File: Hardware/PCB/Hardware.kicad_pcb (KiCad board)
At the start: 2 copper layers, 68.6 x 53.3 mm, 33 parts, among them J1 Conn_01x03_Male, M1 Motor_Servo, M2 Motor_Servo, M3 Motor_Servo, P1 Power, P2 Analog, P3 Digital, P4 Digital, P5 CONN_01X01, P6 CONN_01X01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

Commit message: Nouveau PCB simplifié
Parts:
- removed RV1: R_POT, Potentiometer_THT:Potentiometer_Alps_RK09L_Single_Vertical
- removed SW1: SW_Push, Button_Switch_THT:SW_PUSH_6mm
- added R11: R, Resistor_THT:R_Axial_DIN0204_L3.6mm_D1.6mm_P2.54mm_Vertical, F.Cu at (174.5, 84.5)
- BZ1: footprint Buzzer_Beeper:MagneticBuzzer_Kingstate_KCG0601 -> Connector_PinHeader_2.54mm:PinHeader_1x02_P2.54mm_Horizontal
- R1: footprint Resistor_THT:R_Axial_DIN0204_L3.6mm_D1.6mm_P1.90mm_Vertical -> Resistor_THT:R_Axial_DIN0204_L3.6mm_D1.6mm_P2.54mm_Vertical
- R2, R4, R6, R8: footprint Connector_JST:JST_XH_B02B-XH-A_1x02_P2.50mm_Vertical -> Connector_PinHeader_2.54mm:PinHeader_1x02_P2.54mm_Vertical
- moved D4 63.6 mm to (174.5, 81.4)
- moved R10 48.6 mm to (156.7, 84.5), turned to 270 degrees
- moved D5 42.8 mm to (156.7, 81.9)
- moved R1 36.0 mm to (154.2, 89.5), turned to 180 degrees
- moved U3 26.4 mm to (132.6, 111.1)
- moved D1 25.3 mm to (145.3, 108.6), turned to 90 degrees
- moved R2 21.7 mm to (164.3, 107.3), turned to 0 degrees
- moved R6 18.0 mm to (168.1, 107.3), turned to 0 degrees
- moved M3 17.6 mm to (175.8, 97.2), turned to 270 degrees
- moved U1 15.2 mm to (132.6, 98.4), turned to 0 degrees
- moved BZ1 14.9 mm to (155.4, 98.4), turned to 0 degrees
- moved R8 14.2 mm to (172.0, 107.3), turned to 0 degrees
- moved R4 12.7 mm to (160.5, 107.3), turned to 0 degrees
- moved R9 12.0 mm to (169.4, 120.0), turned to 0 degrees
- moved D3 10.5 mm to (145.3, 95.9), turned to 90 degrees
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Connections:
- D4 pad 2: /7 -> /2
- D5 pad 1: Net-(D4-Pad1) -> Net-(D5-Pad1)
- J1 pad 1: Net-(J1-Pad1) -> +5V
- M1 pad 2: Net-(M1-Pad2) -> +5V
- M2 pad 2: Net-(M1-Pad2) -> +5V
- M3 pad 2: Net-(M1-Pad2) -> +5V
- P3 pad 5: /13(SCK) -> Net-(P3-Pad5)
- R1 pad 1: /A4(SDA) -> Net-(BZ1-Pad1)
- R1 pad 2: Net-(J1-Pad2) -> /9(**)
- R10 pad 1: Net-(D4-Pad1) -> Net-(D5-Pad1)
- R2 pad 1: /13(SCK) -> +5V
- R4 pad 1: /13(SCK) -> +5V
- R6 pad 1: /13(SCK) -> +5V
- R8 pad 1: /13(SCK) -> +5V
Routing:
- net +5V: track 67.8 -> 157.7 mm, vias 2 -> 0
- net /13(SCK): track 69.4 -> 0.00 mm
- net /12(MISO): track 64.0 -> 0.00 mm
- net /7: track 67.1 -> 3.81 mm, vias 2 -> 0
- net /A4(SDA): track 38.2 -> 0.15 mm
- net Net-(M1-Pad2): track 32.3 -> 0.00 mm
- net /8: track 15.1 -> 45.9 mm
- net /3(**): track 51.0 -> 25.3 mm
- net /9(**): track 37.9 -> 18.2 mm
- net /A1: track 28.6 -> 14.0 mm
- net Net-(BZ1-Pad1): track 23.0 -> 9.42 mm
- net Net-(J1-Pad2): track 10.8 -> 0.00 mm
- net Net-(D4-Pad1): track 13.4 -> 3.03 mm
- net /A2: track 24.2 -> 14.5 mm
- net /10(**/SS): track 26.0 -> 35.6 mm
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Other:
- net class Default: trace_width 0.25 -> 0.4

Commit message: PCB corrigé et verifié. Typon prêt
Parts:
- added R12: R, Resistor_THT:R_Axial_DIN0204_L3.6mm_D1.6mm_P5.08mm_Horizontal, F.Cu at (145.3, 93.3)
- added R13: R, Resistor_THT:R_Axial_DIN0204_L3.6mm_D1.6mm_P5.08mm_Horizontal, F.Cu at (145.3, 106.0)
- added R14: R, Resistor_THT:R_Axial_DIN0204_L3.6mm_D1.6mm_P5.08mm_Horizontal, F.Cu at (128.8, 90.8)
- D1, D3: footprint Diode_THT:D_DO-15_P5.08mm_Vertical_KathodeUp -> Diode_THT:D_T-1_P10.16mm_Horizontal
- D2: footprint Diode_THT:D_A-405_P5.08mm_Vertical_KathodeUp -> Diode_THT:D_T-1_P10.16mm_Horizontal
- J1: footprint Connector_PinHeader_1.27mm:PinHeader_1x03_P1.27mm_Horizontal -> Connector_PinHeader_2.54mm:PinHeader_1x03_P2.54mm_Horizontal
- R3, R7: footprint Resistor_THT:R_Axial_DIN0204_L3.6mm_D1.6mm_P1.90mm_Vertical -> Resistor_THT:R_Axial_DIN0204_L3.6mm_D1.6mm_P5.08mm_Horizontal
- moved M3 18.1 mm to (164.3, 83.2), turned to 0 degrees
- moved M1 8.89 mm to (161.8, 90.8)
- moved D3 8.03 mm to (137.7, 93.3), turned to 180 degrees
- moved D1 8.03 mm to (137.7, 106.0), turned to 180 degrees
- moved D2 8.03 mm to (137.7, 81.9), turned to 180 degrees
- moved M2 8.03 mm to (159.3, 98.4)
- moved BZ1 6.48 mm to (154.2, 104.8), turned to 270 degrees
- moved R1 3.81 mm to (154.2, 93.3)
- moved R7 1.27 mm to (168.1, 114.9)
- moved R3 1.27 mm to (163.1, 114.9)
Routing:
- net /12(MISO): track 0.00 -> 41.8 mm
- net /3(**): track 25.3 -> 8.90 mm
- net +5V: track 157.7 -> 142.5 mm
- net /5(**): track 6.35 -> 15.2 mm
- net /6(**): track 16.3 -> 22.9 mm
- net Net-(D2-Pad1): track 9.98 -> 4.08 mm
- net /8: track 45.9 -> 49.7 mm
- net /9(**): track 18.2 -> 22.0 mm
- net Net-(D3-Pad1): track 8.83 -> 5.24 mm
- net /11(**/MOSI): track 14.3 -> 17.4 mm
- net /10(**/SS): track 35.6 -> 37.2 mm
- net /A1: track 14.0 -> 15.0 mm
- net Net-(BZ1-Pad1): track 9.42 -> 10.2 mm

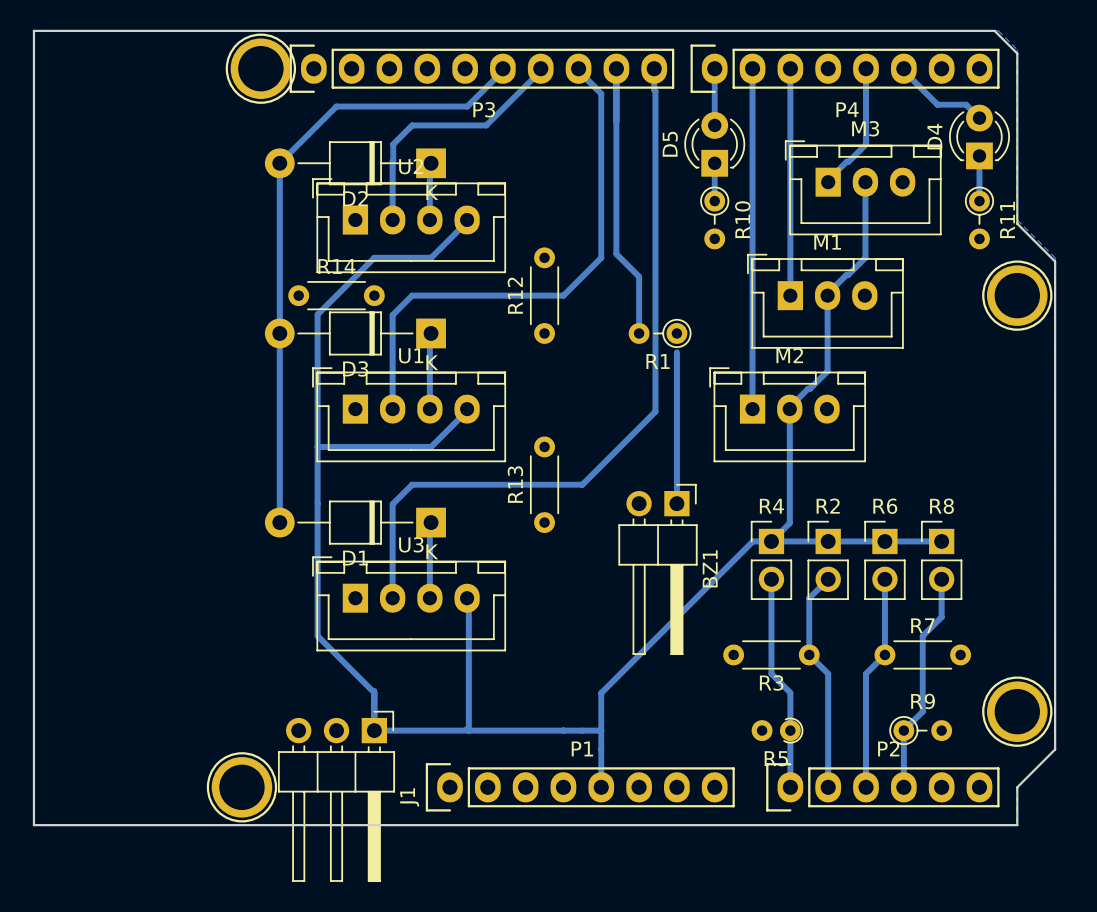
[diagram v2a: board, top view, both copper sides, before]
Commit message: Code testeur UltraSon+Diodes sur PCB Ajout pull down sur la ligne ECHO
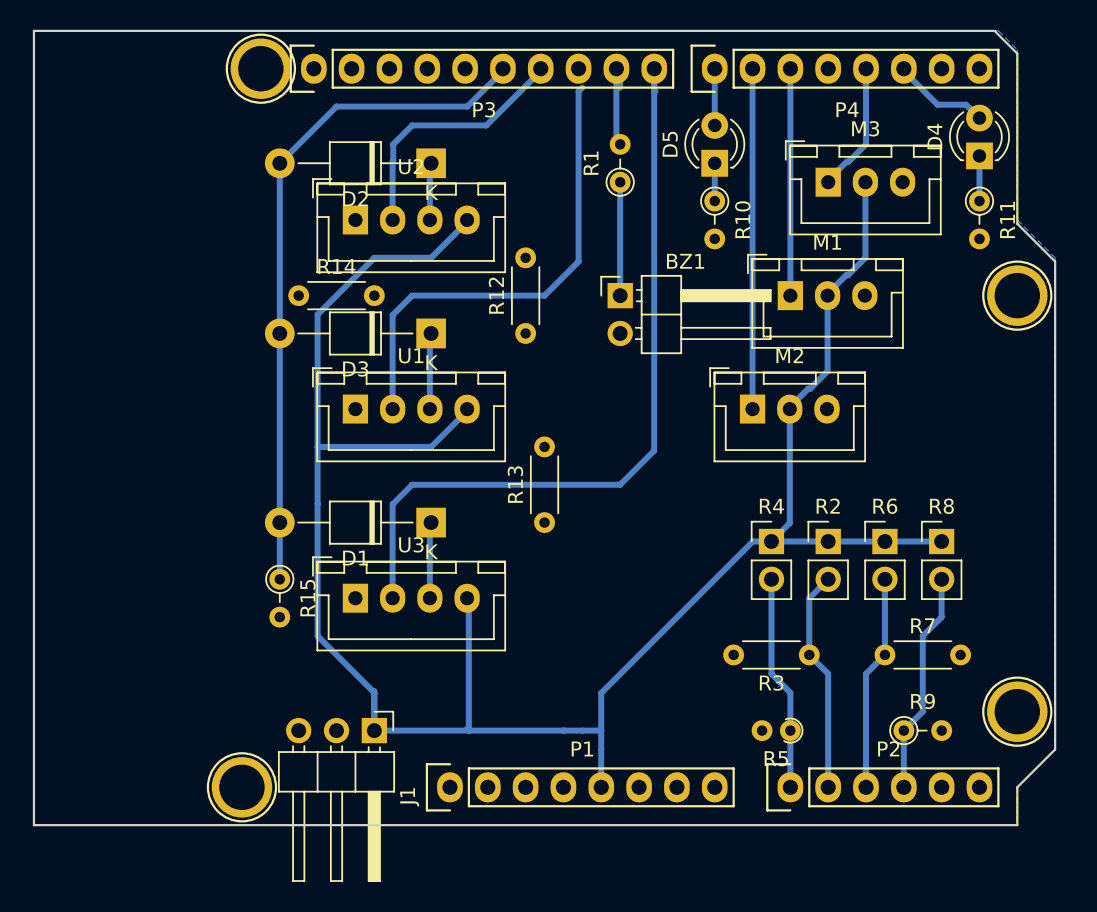
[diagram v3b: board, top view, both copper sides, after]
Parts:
- added R15: R, Resistor_THT:R_Axial_DIN0204_L3.6mm_D1.6mm_P2.54mm_Vertical, F.Cu at (127.5, 109.9)
- moved BZ1 14.5 mm to (150.4, 90.8), turned to 0 degrees
- moved R1 10.9 mm to (150.4, 83.2), turned to 90 degrees
- moved R12 1.27 mm to (144.0, 93.3)
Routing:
- net /9(**): track 22.0 -> 6.56 mm
- net /10(**/SS): track 37.2 -> 32.4 mm
- net /12(MISO): track 41.8 -> 45.6 mm
- net /8: track 49.7 -> 52.7 mm
- net Net-(BZ1-Pad1): track 10.2 -> 7.62 mm

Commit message: Texte sur le pcb pour eviter erreur de gravure
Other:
- net class Default: trace_width 0.4 -> 0.5
- board text added: "BAUDEAU MARTINEZ YJJOU"
- board text added: "Projet MOSH QuanticAnt 2018"
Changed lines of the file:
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@@
   (general
     (thickness 1.6)
-    (drawings 24)
+    (drawings 26)
     (tracks 125)
     (zones 0)
@@
   )
   (setup
-    (last_trace_width 0.4)
+    (last_trace_width 0.5)
     (trace_clearance 0.2)
     (zone_clearance 0.508)
@@
     (mod_text_size 1 1)
     (mod_text_width 0.15)
-    (pad_size 4.064 4.064)
-    (pad_drill 3.048)
+    (pad_size 1.7 1.7)
+    (pad_drill 0.95)
     (pad_to_mask_clearance 0)
     (aux_axis_origin 110.998 126.365)
@@
   (net_class Default "This is the default net class."
     (clearance 0.2)
-    (trace_width 0.4)
+    (trace_width 0.5)
     (via_dia 0.6)
     (via_drill 0.4)
@@
     (pad 1 thru_hole circle (at 0 0) (size 4.064 4.064) (drill 3.048) (layers *.Cu *.Mask F.SilkS)
       (net 25 "Net-(P7-Pad1)"))
+  )
+  (gr_text "BAUDEAU MARTINEZ YJJOU" (at 121.158 97.155 90) (layer B.Cu)
+    (effects (font (size 1.5 1.5) (thickness 0.3)) (justify mirror))
+  )
+  (gr_text "Projet MOSH\nQuanticAnt 2018" (at 116.078 97.155 90) (layer B.Cu)
+    (effects (font (size 1.5 1.5) (thickness 0.3)) (justify mirror))
   )
   (gr_line (start 120.523 93.98) (end 104.648 93.98) (angle 90) (layer Dwgs.User) (width 0.15))
@@
   (segment (start 130.048 104.775) (end 130.048 100.965) (width 0.4) (layer B.Cu) (net 3))
   (segment (start 159.278 107.315) (end 160.528 107.315) (width 0.4) (layer B.Cu) (net 3))
-  (segment (start 149.098 117.495) (end 159.278 107.315) (width 0.4) (layer B.Cu) (net 3))
   (segment (start 147.828 120.015) (end 149.098 120.015) (width 0.4) (layer B.Cu) (net 3))
   (segment (start 149.098 121.285) (end 149.098 120.015) (width 0.4) (layer B.Cu) (net 3))
@@
   (segment (start 133.858 88.265) (end 137.673 88.265) (width 0.4) (layer B.Cu) (net 3))
   (segment (start 137.673 88.265) (end 140.088 85.85) (width 0.4) (layer B.Cu) (net 3))
+  (segment (start 149.098 117.495) (end 159.278 107.315) (width 0.4) (layer B.Cu) (net 3))
   (segment (start 160.528 109.855) (end 160.528 116.205) (width 0.4) (layer B.Cu) (net 6))
   (segment (start 161.798 117.475) (end 161.798 120.015) (width 0.4) (layer B.Cu) (net 6))
@@
     (polygon
       (pts
-        (xy 110.998 73.025) (xy 175.768 73.025) (xy 177.038 74.295) (xy 177.038 85.725) (xy 179.578 88.265)
-        (xy 179.578 121.285) (xy 177.038 123.825) (xy 177.038 126.365) (xy 110.998 126.365)
+        (xy 175.768 73.025) (xy 177.038 74.295) (xy 177.038 85.725) (xy 179.578 88.265) (xy 179.578 121.285)
+        (xy 177.038 123.825) (xy 177.038 126.365) (xy 110.998 126.365) (xy 110.998 73.025)
       )
     )
